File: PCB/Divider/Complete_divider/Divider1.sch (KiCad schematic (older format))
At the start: 57 parts, among them J2 15kV, J3 Electr.

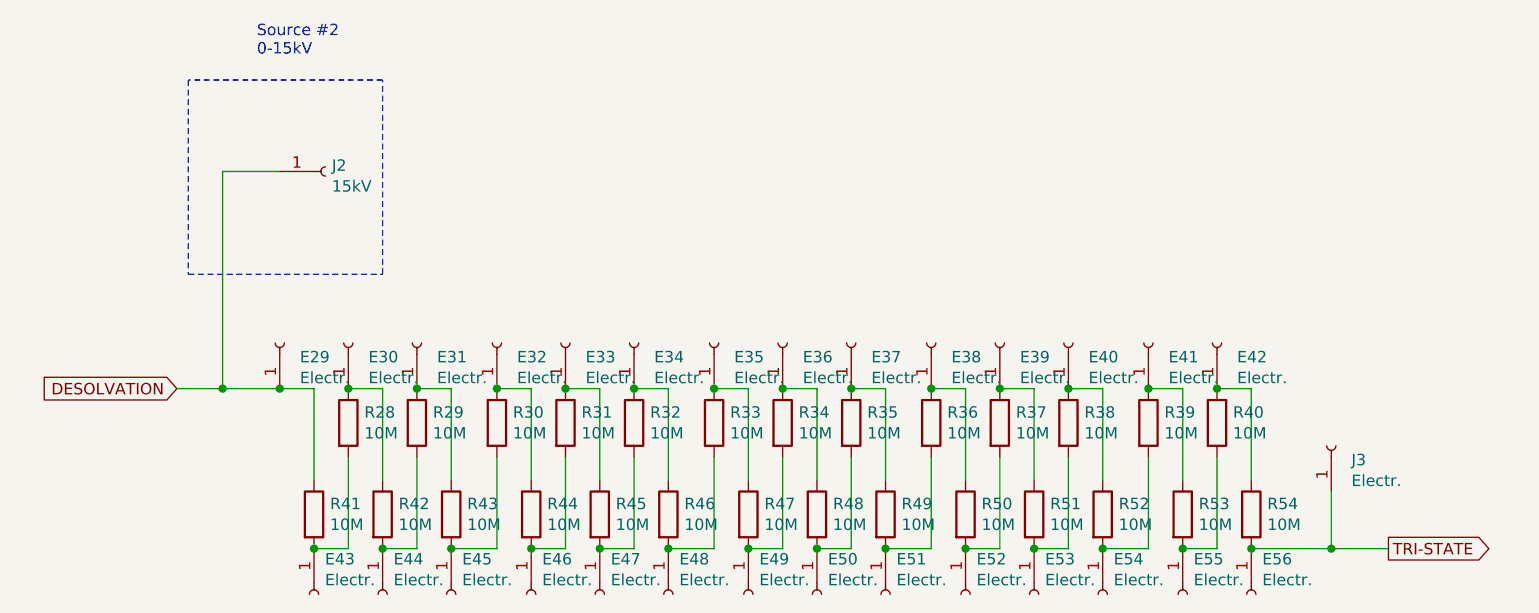
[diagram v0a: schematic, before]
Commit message: Updates of dividers 1 & 2
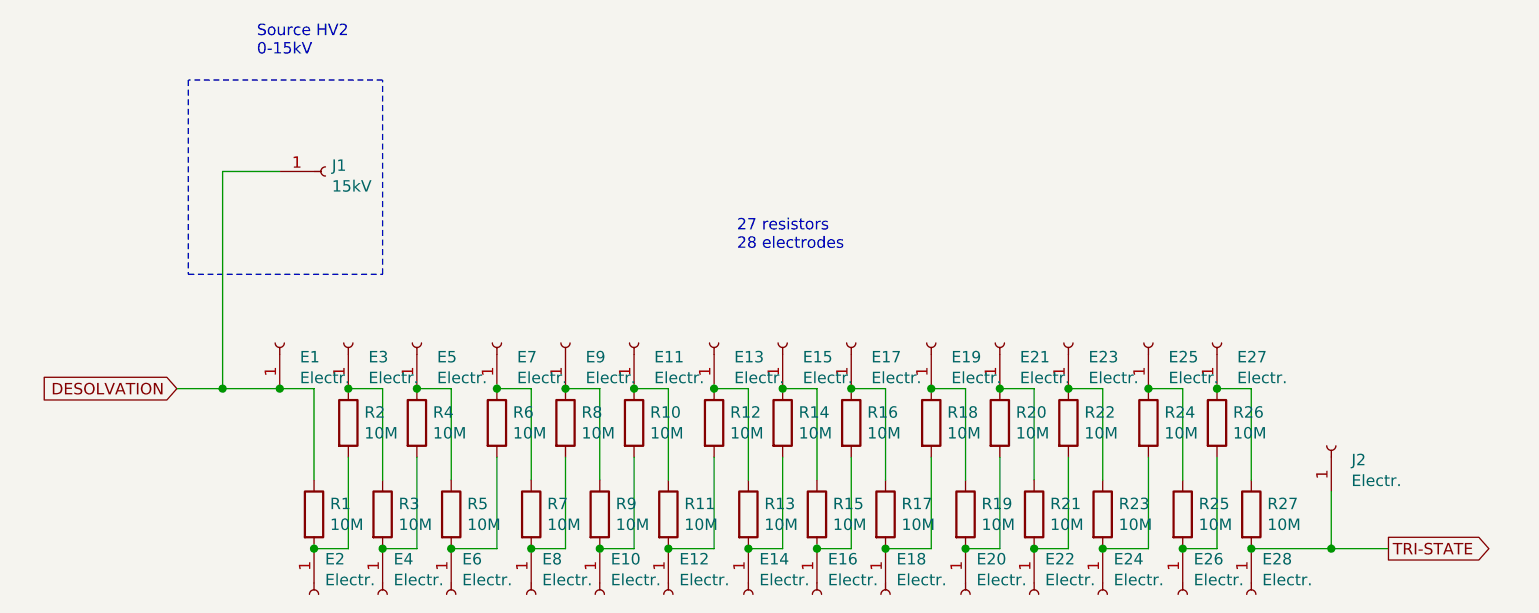
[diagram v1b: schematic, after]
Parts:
- renumbered E29 to E1, E47 to E10, E34 to E11, E48 to E12, E35 to E13, E49 to E14, E36 to E15, E50 to E16, E37 to E17, E51 to E18, E38 to E19, E43 to E2, E52 to E20, E39 to E21, E53 to E22, E40 to E23, E54 to E24, E41 to E25, E55 to E26, E42 to E27, E56 to E28, E30 to E3, E44 to E4, E31 to E5, E45 to E6, E32 to E7, E46 to E8, E33 to E9, J2 to J1, J3 to J2, R41 to R1, R32 to R10, R46 to R11, R33 to R12, R47 to R13, R34 to R14, R48 to R15, R35 to R16, R49 to R17, R36 to R18, R50 to R19, R28 to R2, R37 to R20, R51 to R21, R38 to R22, R52 to R23, R39 to R24, R53 to R25, R40 to R26, R54 to R27, R42 to R3, R29 to R4, R43 to R5, R30 to R6, R44 to R7, R31 to R8, R45 to R9
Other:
- note added: "27 resistors \n28 electrodes"
- note added: "Source HV2 \n0-15kV\n"
- note removed: "Source #2 \n0-15kV\n"
